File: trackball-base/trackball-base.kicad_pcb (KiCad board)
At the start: 4 copper layers, 110 x 140 mm, 159 parts, among them J201 TYPE-C-31-M-12, J202 CORTEX-DBG-10, Q101 2N7002, SW201 RESET, SW202 BOOT, SW401 D2FC-F-7N, SW402 D2FC-F-7N, SW403 D2FC-F-7N, U101 AP2112K-3.3TRG1, U102 APX809-29SAG-7, U103 XC6206P192MR, U104 TPS22918DBVR, U105 TPS22918DBVR, U106 TLV3011AIDBVR, U107 TLV3011AIDBVR, U201 E73-2G4M08S1C, U202 TPD2E1B06DRLR, U301 PMW3360DM-T2QU, U302 PMW3360DM-T2QU, U501 LTC4125EUFD, Y201 ABS07-32.768KHZ-9-T

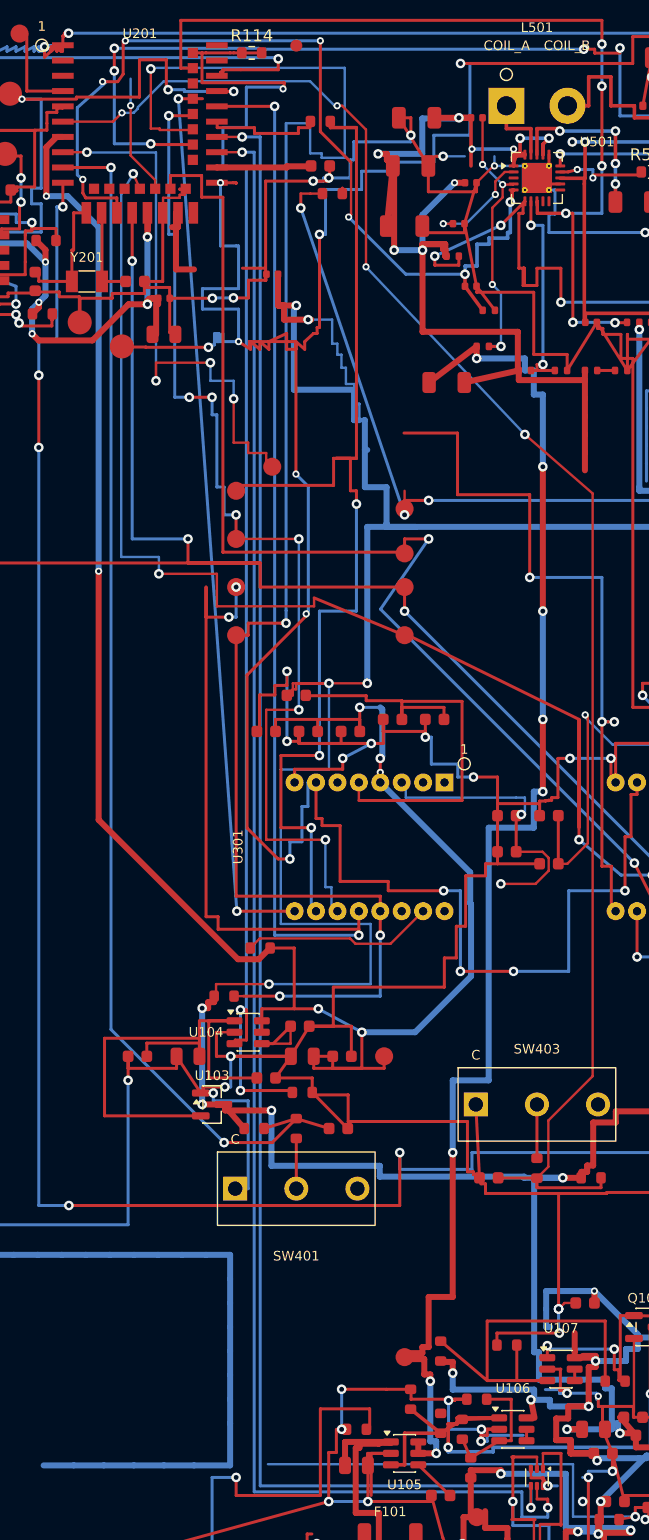
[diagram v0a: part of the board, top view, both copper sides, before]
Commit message: Wave-4a VBUS_SENSE CLOSED drc205 12unc/0err/0parity (east-jog + In2 slalom x16.50/BTN2-bypass)
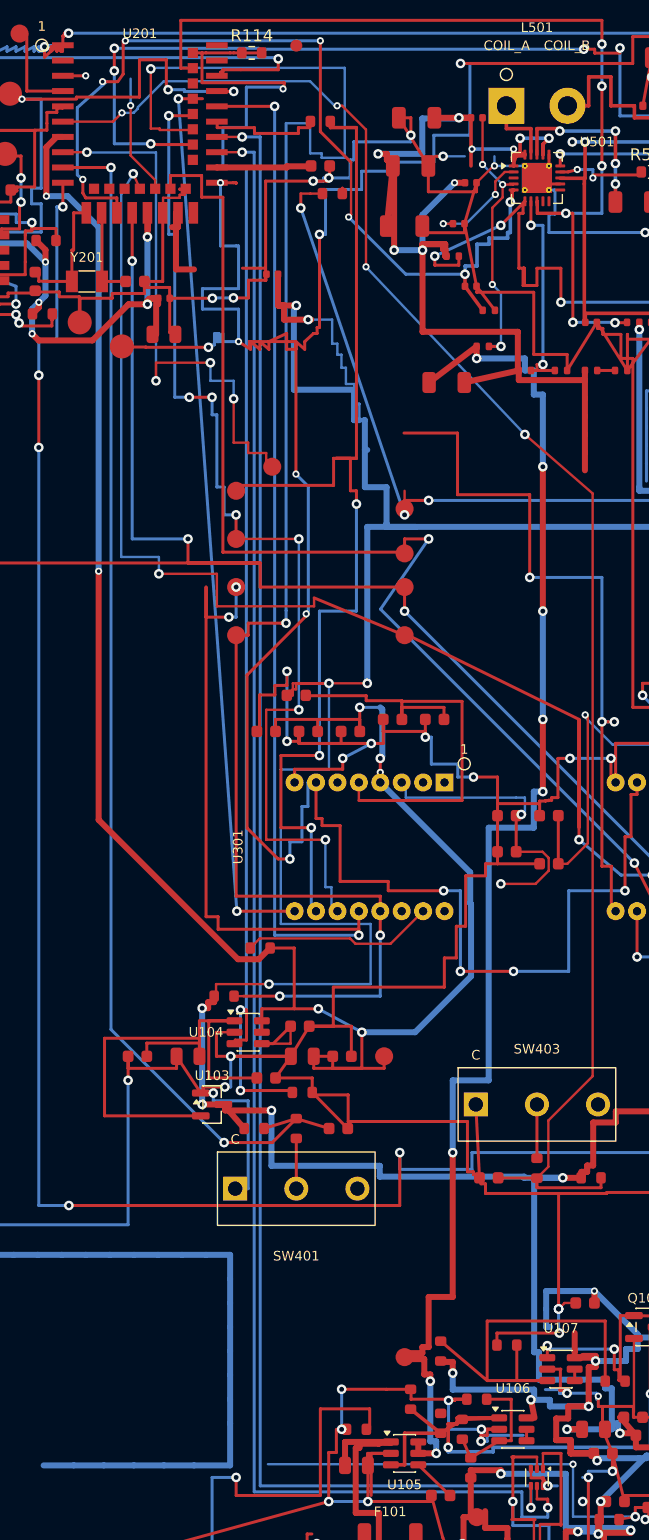
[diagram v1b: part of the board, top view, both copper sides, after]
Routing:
- net VBUS_SENSE: track 74.7 -> 234.6 mm, vias 7 -> 9
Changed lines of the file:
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@@
+	)
+	(segment
+		(start 16.5 7.51)
+		(end 17.5 7.51)
+		(width 0.25)
+		(layer "F.Cu")
+		(net "VBUS_SENSE")
 	)
 	(segment
@@
 	)
 	(via
+		(at 58 122.9)
+		(size 0.6)
+		(drill 0.3)
+		(layers "F.Cu" "B.Cu")
+		(net "VBUS_SENSE")
+	)
+	(via
 		(at 91 126)
 		(size 0.8)
@@
 	(via
 		(at 76.2 126)
+		(size 0.6)
+		(drill 0.3)
+		(layers "F.Cu" "B.Cu")
+		(net "VBUS_SENSE")
+	)
+	(via
+		(at 17.5 7.51)
 		(size 0.6)
 		(drill 0.3)
@@
 		(net "VBUS_SENSE")
 	)
+	(segment
+		(start 17.5 7.51)
+		(end 16.5 7.51)
+		(width 0.25)
+		(layer "In2.Cu")
+		(net "VBUS_SENSE")
+	)
+	(segment
+		(start 17 100.5)
+		(end 17 102.3)
+		(width 0.25)
+		(layer "In2.Cu")
+		(net "VBUS_SENSE")
+	)
+	(segment
+		(start 17 102.3)
+		(end 16.5 102.3)
+		(width 0.25)
+		(layer "In2.Cu")
+		(net "VBUS_SENSE")
+	)
+	(segment
+		(start 16.5 100.5)
+		(end 17 100.5)
+		(width 0.25)
+		(layer "In2.Cu")
+		(net "VBUS_SENSE")
+	)
+	(segment
+		(start 16.5 122.9)
+		(end 58 122.9)
+		(width 0.25)
+		(layer "In2.Cu")
+		(net "VBUS_SENSE")
+	)
+	(segment
+		(start 16.5 7.51)
+		(end 16.5 100.5)
+		(width 0.25)
+		(layer "In2.Cu")
+		(net "VBUS_SENSE")
+	)
+	(segment
+		(start 16.5 102.3)
+		(end 16.5 122.9)
+		(width 0.25)
+		(layer "In2.Cu")
+		(net "VBUS_SENSE")
+	)

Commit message: Wave-4b VIN east link CLOSED via grand tour drc208 11unc/0err/0parity (In2 x55/x40/@4.00/x73.49, pad3 only VIN left)
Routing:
- net VIN: track 127.1 -> 195.2 mm
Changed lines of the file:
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@@
+	)
+	(segment
+		(start 40 4)
+		(end 73.49 4)
+		(width 0.3)
+		(layer "In2.Cu")
+		(net "VIN")
+	)
+	(segment
+		(start 40 8.1)
+		(end 40 4)
+		(width 0.3)
+		(layer "In2.Cu")
+		(net "VIN")
+	)
+	(segment
+		(start 56 12.7)
+		(end 55 12.7)
+		(width 0.3)
+		(layer "In2.Cu")
+		(net "VIN")
+	)
+	(segment
+		(start 55 12.7)
+		(end 55 8.1)
+		(width 0.3)
+		(layer "In2.Cu")
+		(net "VIN")
+	)
+	(segment
+		(start 55 8.1)
+		(end 40 8.1)
+		(width 0.3)
+		(layer "In2.Cu")
+		(net "VIN")
+	)
+	(segment
+		(start 73.49 4)
+		(end 73.49 14)
+		(width 0.3)
+		(layer "In2.Cu")
+		(net "VIN")
 	)
 	(segment

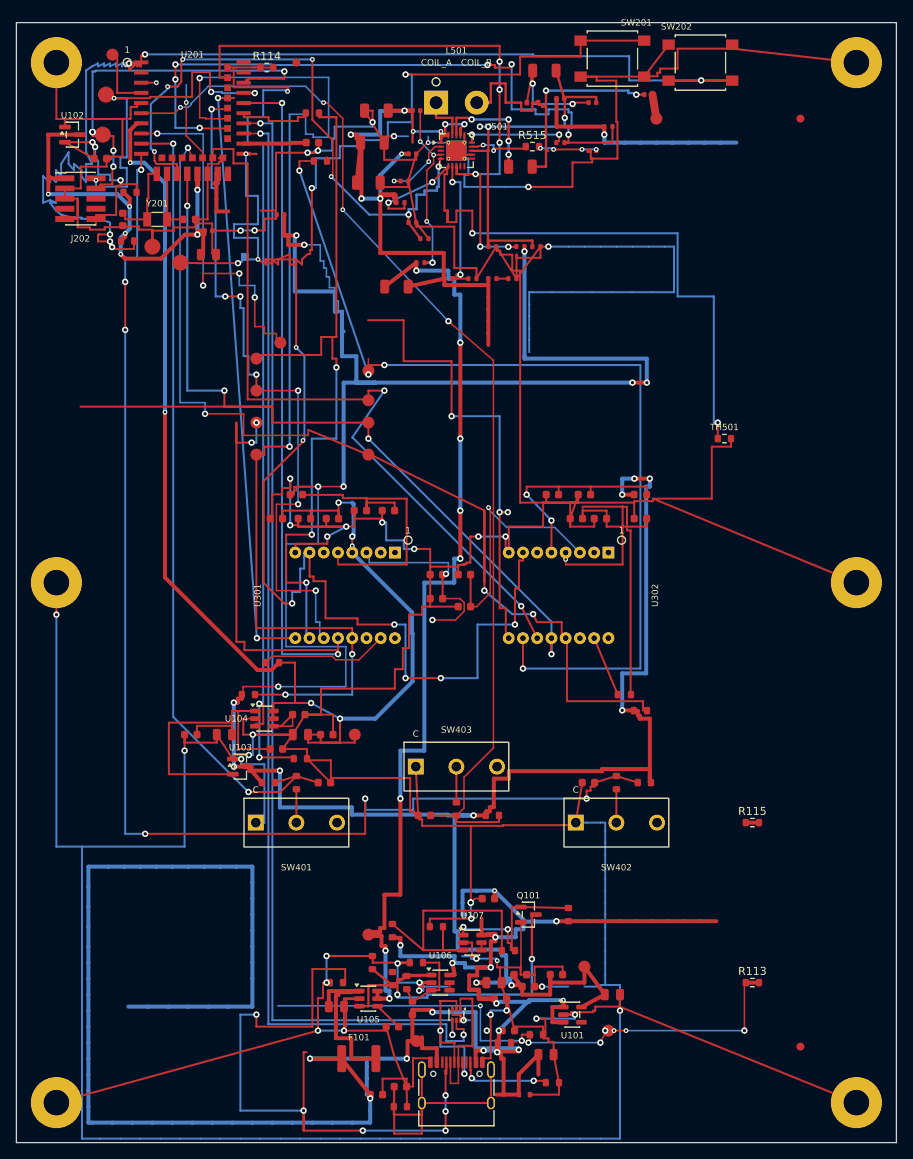
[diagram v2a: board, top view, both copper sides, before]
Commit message: Wave-4c MCU_TX_EN CLOSED drc211 9unc/0err/0parity (F-escape v3 + In2 N-S x24.60 + E-W @119.10 + riser x91.175, 2 via-in-pad)
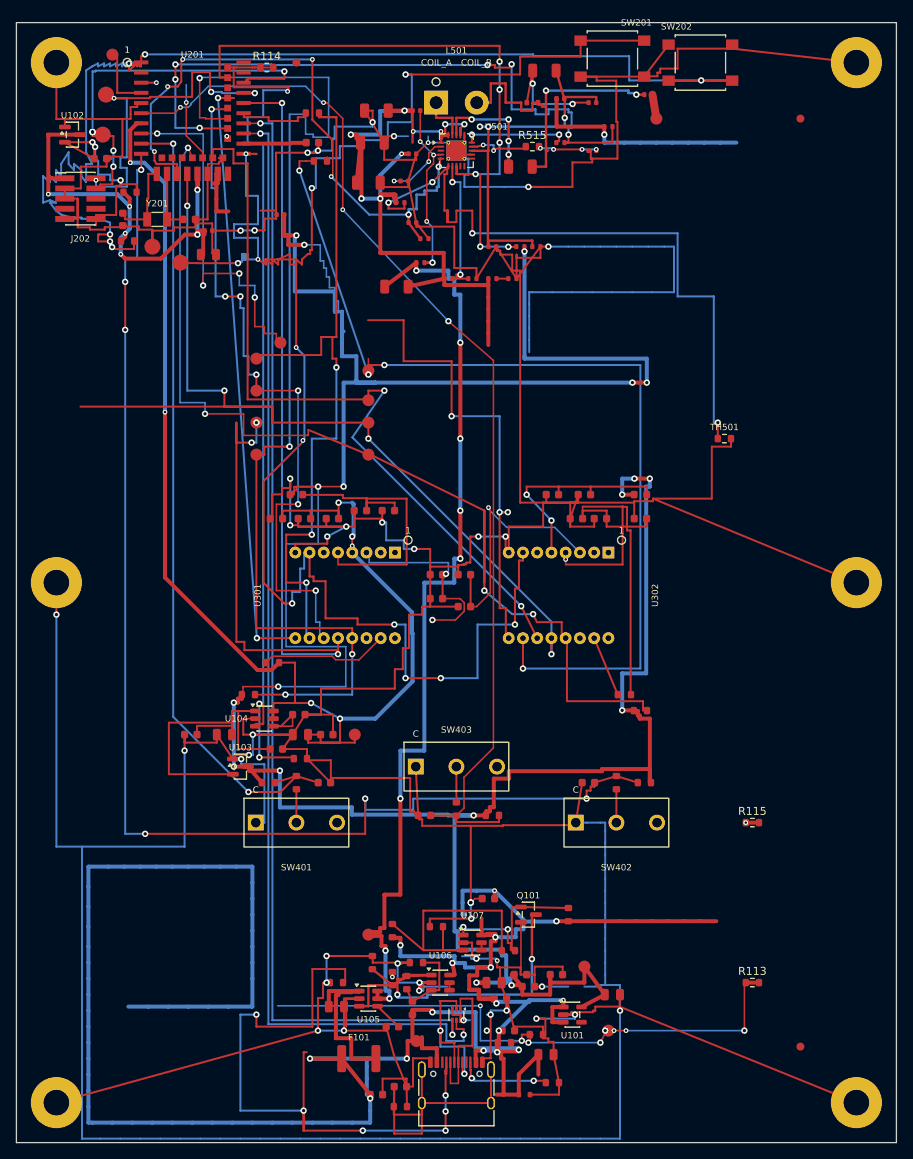
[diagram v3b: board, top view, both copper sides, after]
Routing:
- net MCU_TX_EN: track 1.65 -> 194.5 mm, vias 0 -> 3
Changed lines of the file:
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@@
+	)
+	(segment
+		(start 47 119.08)
+		(end 47 119.3)
+		(width 0.25)
+		(layer "F.Cu")
+		(net "MCU_TX_EN")
+	)
+	(via
+		(at 47 119.3)
+		(size 0.6)
+		(drill 0.3)
+		(layers "F.Cu" "B.Cu")
+		(net "MCU_TX_EN")
+	)
+	(via
+		(at 91.175 100)
+		(size 0.6)
+		(drill 0.3)
+		(layers "F.Cu" "B.Cu")
+		(net "MCU_TX_EN")
+	)
+	(via
+		(at 26.3 14.2)
+		(size 0.6)
+		(drill 0.3)
+		(layers "F.Cu" "B.Cu")
+		(net "MCU_TX_EN")
+	)
+	(segment
+		(start 47 118.675)
+		(end 47 119.3)
+		(width 0.25)
+		(layer "In2.Cu")
+		(net "MCU_TX_EN")
+	)
+	(segment
+		(start 47 119.1)
+		(end 47 119.3)
+		(width 0.25)
+		(layer "In2.Cu")
+		(net "MCU_TX_EN")
+	)
+	(segment
+		(start 91.175 119.1)
+		(end 91.175 100)
+		(width 0.25)
+		(layer "In2.Cu")
+		(net "MCU_TX_EN")
+	)
+	(segment
+		(start 24.6 14.2)
+		(end 24.6 118.675)
+		(width 0.25)
+		(layer "In2.Cu")
+		(net "MCU_TX_EN")
+	)
+	(segment
+		(start 47 119.1)
+		(end 91.175 119.1)
+		(width 0.25)
+		(layer "In2.Cu")
+		(net "MCU_TX_EN")
+	)
+	(segment
+		(start 26.3 14.2)
+		(end 24.6 14.2)
+		(width 0.25)
+		(layer "In2.Cu")
+		(net "MCU_TX_EN")
+	)
+	(segment
+		(start 24.6 118.675)
+		(end 47 118.675)
+		(width 0.25)
+		(layer "In2.Cu")
+		(net "MCU_TX_EN")
 	)
 	(segment

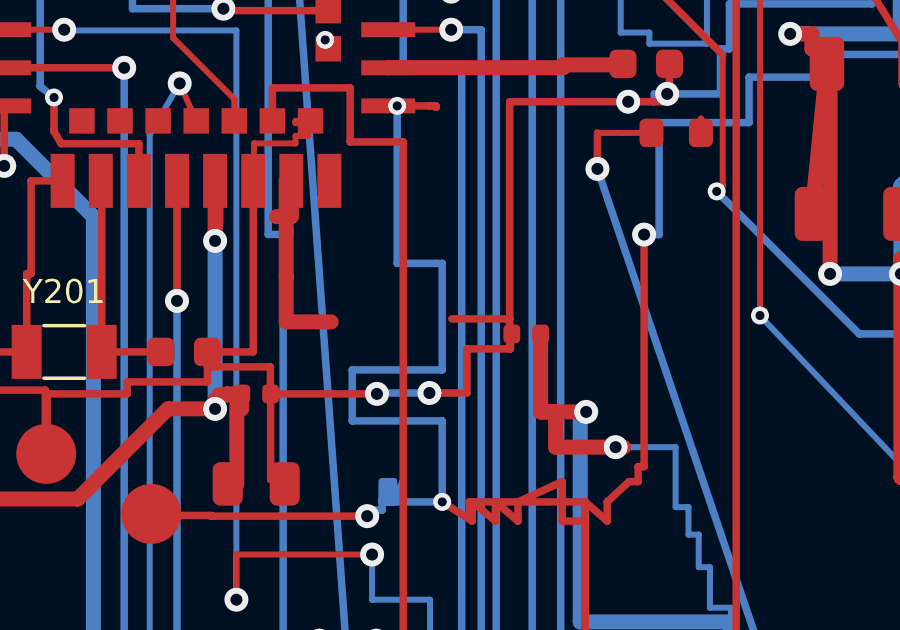
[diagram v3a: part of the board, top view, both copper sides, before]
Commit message: Wave-5 +3V3 gap-b CLOSED, gap-a parked SEALED drc222 8unc/0err/0parity (GND-rail ECO rejected: load-bearing; maze-spine sealed all layers)
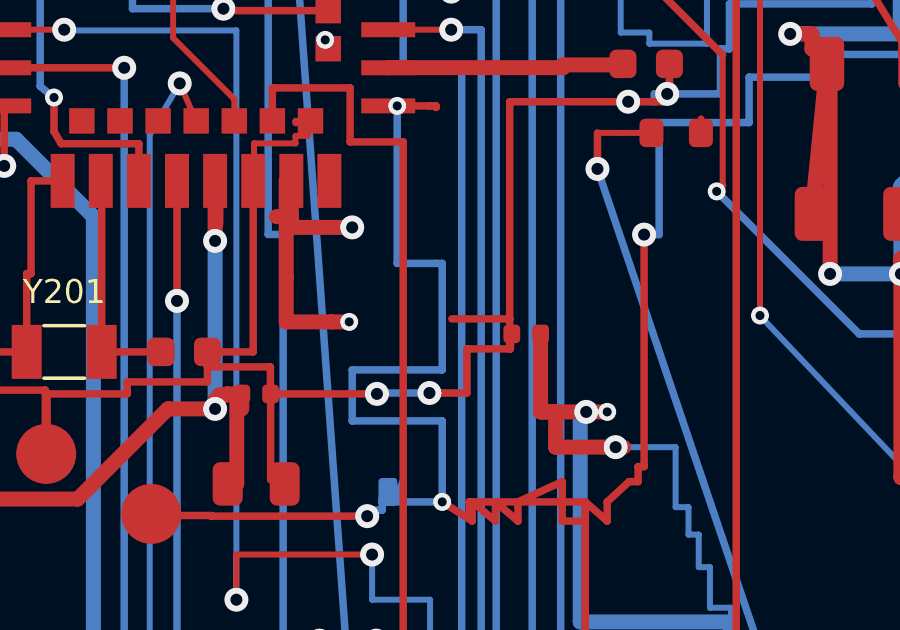
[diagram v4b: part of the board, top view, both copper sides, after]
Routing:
- net +3V3: track 455.5 -> 470.8 mm, vias 24 -> 27
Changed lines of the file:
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@@
 	)
 	(segment
+		(start 25.17 20.09)
+		(end 25.17 20.45)
+		(width 0.5)
+		(layer "F.Cu")
+		(net "+3V3")
+	)
+	(segment
 		(start 34.712 59)
 		(end 34.212 59)
@@
 	)
 	(segment
+		(start 26.5 23.6)
+		(end 27.1 23.6)
+		(width 0.5)
+		(layer "F.Cu")
+		(net "+3V3")
+	)
+	(segment
 		(start 6.05 19.46)
 		(end 4.3983 19.46)
@@
 	)
 	(segment
+		(start 35 26.6)
+		(end 35.7 26.6)
+		(width 0.5)
+		(layer "F.Cu")
+		(net "+3V3")
+	)
+	(segment
 		(start 58.675 99.1)
 		(end 57.15 99.1)
@@
 	)
 	(segment
+		(start 25.17 20.45)
+		(end 27.2 20.45)
+		(width 0.5)
+		(layer "F.Cu")
+		(net "+3V3")
+	)
+	(segment
 		(start 28.963 93)
 		(end 28.938 93)
@@
 	)
 	(via
+		(at 27.1 23.6)
+		(size 0.6)
+		(drill 0.3)
+		(layers "F.Cu" "B.Cu")
+		(net "+3V3")
+	)
+	(via
 		(at 14.1542 22.9815)
 		(size 0.6)
@@
 	)
 	(via
+		(at 35.7 26.6)
+		(size 0.6)
+		(drill 0.3)
+		(layers "F.Cu" "B.Cu")
+		(net "+3V3")
+	)
+	(via
+		(at 27.2 20.45)
+		(size 0.8)
+		(drill 0.4)
+		(layers "F.Cu" "B.Cu")
+		(net "+3V3")
+	)
+	(via
 		(at 57.5 120)
 		(size 0.8)
@@
 	)
 	(segment
+		(start 27.1 23.6)
+		(end 35.7 23.6)
+		(width 0.5)
+		(layer "In2.Cu")
+		(net "+3V3")
+	)
+	(segment
+		(start 35.7 23.6)
+		(end 35.7 26.6)
+		(width 0.5)
+		(layer "In2.Cu")
+		(net "+3V3")
+	)
+	(segment
 		(start 60.325 99.925)
 		(end 60.325 99.1)
@@
 	)
 	(segment
+		(start 23.9 18.9)
+		(end 23.9 24.6)
+		(width 0.25)
+		(layer "F.Cu")
+		(net "GND")
+	)
+	(segment
 		(start 45.475 20.55)
 		(end 45.475 20)
@@
 		(width 0.25)
 		(layer "F.Cu")
-		(net "GND")
-	)
-	(segment
-		(start 23.9 18.9)
-		(end 23.9 24.6)
-		(width 0.25)
-		(layer "F.Cu")

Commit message: Wave-6 GND CLOSED drc225 7unc/0err/0parity (In2 direct (55.90,124.70)->(59.27,124.00); B south/north-arounds dead on VBUS-rail+SENSE)
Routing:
- net GND: track 1188.4 -> 1192.5 mm
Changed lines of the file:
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@@
+	)
+	(segment
+		(start 55.9 124.7)
+		(end 59.27 124.7)
+		(width 0.25)
+		(layer "In2.Cu")
+		(net "GND")
+	)
+	(segment
+		(start 59.27 124.7)
+		(end 59.27 124)
+		(width 0.25)
+		(layer "In2.Cu")
+		(net "GND")
 	)
 	(segment

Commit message: Wave-8 MCU_RST CLOSED drc230 6unc/0err/0parity (B-rail+existing-via west, F-hop over SENSE-spine, F-step to @30.05 maze)
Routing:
- net MCU_RST: track 272.8 -> 295.8 mm, vias 15 -> 18
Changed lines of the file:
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@@
+	)
+	(segment
+		(start 22.3 30.05)
+		(end 22.3 31)
+		(width 0.25)
+		(layer "F.Cu")
+		(net "MCU_RST")
 	)
 	(segment
 		(start 36.64 66.24)
 		(end 36.64 69.24)
+		(width 0.25)
+		(layer "F.Cu")
+		(net "MCU_RST")
+	)
+	(segment
+		(start 22.3 31)
+		(end 22.3 31.6)
 		(width 0.25)
 		(layer "F.Cu")
@@
 	)
 	(segment
+		(start 15.7 31.3)
+		(end 17.3 31.3)
+		(width 0.25)
+		(layer "F.Cu")
+		(net "MCU_RST")
+	)
+	(segment
 		(start 34.97 29.6)
 		(end 31.1 29.6)
@@
 	)
 	(segment
+		(start 21.5 31)
+		(end 22.3 31)
+		(width 0.25)
+		(layer "F.Cu")
+		(net "MCU_RST")
+	)
+	(segment
 		(start 32.725 29.6)
 		(end 34.2 28.925)
@@
 		(size 0.8)
 		(drill 0.4)
+		(layers "F.Cu" "B.Cu")
+		(net "MCU_RST")
+	)
+	(via
+		(at 17.3 31)
+		(size 0.6)
+		(drill 0.3)
 		(layers "F.Cu" "B.Cu")
 		(net "MCU_RST")
@@
 	)
 	(via
+		(at 15.7 31)
+		(size 0.6)
+		(drill 0.3)
+		(layers "F.Cu" "B.Cu")
+		(net "MCU_RST")
+	)
+	(via
 		(at 30.2 29.6)
 		(size 0.6)
@@
 		(net "MCU_RST")
 	)
+	(via
+		(at 22.4 31)
+		(size 0.6)
+		(drill 0.3)
+		(layers "F.Cu" "B.Cu")
+		(net "MCU_RST")
+	)
 	(segment
 		(start 27.2 26.9)
@@
 		(net "MCU_RST")
 	)
+	(segment
+		(start 14.9 31)
+		(end 15.7 31)
+		(width 0.25)
+		(layer "In2.Cu")
+		(net "MCU_RST")
+	)
+	(segment
+		(start 13.025 19.705)
+		(end 13.025 22.1)
+		(width 0.25)
+		(layer "In2.Cu")
+		(net "MCU_RST")
+	)
+	(segment
+		(start 17.3 31)
+		(end 22.3 31)
+		(width 0.25)
+		(layer "In2.Cu")
+		(net "MCU_RST")
+	)
+	(segment
+		(start 14.9 22.1)
+		(end 14.9 31)
+		(width 0.25)
+		(layer "In2.Cu")
+		(net "MCU_RST")
+	)
+	(segment
+		(start 13.025 22.1)
+		(end 14.9 22.1)
+		(width 0.25)
+		(layer "In2.Cu")
+		(net "MCU_RST")
+	)

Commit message: Wave-9 VBUS CLOSED drc234 5unc/0err/0parity (via C205-1 + In2 E-W @15.00 + N-S x31.50 w/ +3V3-tip jog + F-E-W/via at @105.50)
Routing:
- net VBUS: track 320.5 -> 430.3 mm, vias 16 -> 18
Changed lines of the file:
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@@
+	)
+	(segment
+		(start 31.5 105.5)
+		(end 29.5 105.5)
+		(width 0.5)
+		(layer "F.Cu")
+		(net "VBUS")
 	)
 	(segment
@@
 	)
 	(via
+		(at 29.5 105.5)
+		(size 0.8)
+		(drill 0.4)
+		(layers "F.Cu" "B.Cu")
+		(net "VBUS")
+	)
+	(via
 		(at 59.875 114.325)
 		(size 0.8)
@@
 	)
 	(via
+		(at 36.23 15)
+		(size 0.8)
+		(drill 0.4)
+		(layers "F.Cu" "B.Cu")
+		(net "VBUS")
+	)
+	(via
 		(at 52 123.7)
 		(size 0.8)
@@
 		(net "VBUS")
 	)
+	(segment
+		(start 31.5 15)
+		(end 31.5 22.7)
+		(width 0.5)
+		(layer "In2.Cu")
+		(net "VBUS")
+	)
+	(segment
+		(start 26.2 24.5)
+		(end 31.5 24.5)
+		(width 0.5)
+		(layer "In2.Cu")
+		(net "VBUS")
+	)
+	(segment
+		(start 31.5 24.5)
+		(end 31.5 105.5)
+		(width 0.5)
+		(layer "In2.Cu")
+		(net "VBUS")
+	)
+	(segment
+		(start 31.5 22.7)
+		(end 26.2 22.7)
+		(width 0.5)
+		(layer "In2.Cu")
+		(net "VBUS")
+	)
+	(segment
+		(start 26.2 22.7)
+		(end 26.2 24.5)
+		(width 0.5)
+		(layer "In2.Cu")
+		(net "VBUS")
+	)
+	(segment
+		(start 36.23 15)
+		(end 31.5 15)
+		(width 0.5)
+		(layer "In2.Cu")
+		(net "VBUS")
+	)
+	(segment
+		(start 29.5 105.5)
+		(end 31.5 105.5)
+		(width 0.5)
+		(layer "In2.Cu")
+		(net "VBUS")
+	)

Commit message: Wave-10 P0.12 CLOSED drc235 4unc/0err/0parity (via B-rail bottom + In2 E-W @7.75 + N-S x39.30 + R207-2 F-step, first-try)
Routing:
- net /mcu/Net-(U201-P0.12): track 10.6 -> 40.7 mm, vias 1 -> 3
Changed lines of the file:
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@@
+	)
+	(segment
+		(start 38.8 17.77)
+		(end 38.8 18.5)
+		(width 0.25)
+		(layer "F.Cu")
+		(net "/mcu/Net-(U201-P0.12)")
 	)
 	(segment
@@
 		(net "/mcu/Net-(U201-P0.12)")
 	)
+	(via
+		(at 21.23 7.75)
+		(size 0.6)
+		(drill 0.3)
+		(layers "F.Cu" "B.Cu")
+		(net "/mcu/Net-(U201-P0.12)")
+	)
+	(via
+		(at 38.8 18.5)
+		(size 0.6)
+		(drill 0.3)
+		(layers "F.Cu" "B.Cu")
+		(net "/mcu/Net-(U201-P0.12)")
+	)
 	(segment
 		(start 21.232 9.988)
@@
 		(net "/mcu/Net-(U201-P0.12)")
 	)
+	(segment
+		(start 39.3 18.5)
+		(end 38.8 18.5)
+		(width 0.25)
+		(layer "In2.Cu")
+		(net "/mcu/Net-(U201-P0.12)")
+	)
+	(segment
+		(start 21.23 7.75)
+		(end 39.3 7.75)
+		(width 0.25)
+		(layer "In2.Cu")
+		(net "/mcu/Net-(U201-P0.12)")
+	)
+	(segment
+		(start 39.3 7.75)
+		(end 39.3 18.5)
+		(width 0.25)
+		(layer "In2.Cu")
+		(net "/mcu/Net-(U201-P0.12)")
+	)
